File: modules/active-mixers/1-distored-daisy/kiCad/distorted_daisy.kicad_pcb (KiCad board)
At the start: 2 copper layers, 90 x 111 mm, 79 parts, among them J1 INPUT_1, J2 INPUT_2, J3 INPUT_3, J4 INPUT_4, J5 OUTPUT, J6 INV_OUT, Q1 BC547, Q2 BC547, Q3 BC547, Q4 BC547, Q5 BC547, U1 TL074

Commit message: add gerber files and ZIPs for V2
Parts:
- moved D3 9.00 mm to (101.0, 71.0)
- moved D4 9.00 mm to (101.0, 89.0)
- moved D5 9.00 mm to (101.0, 107.0)
- moved D6 9.00 mm to (101.0, 125.0)
- moved D7 9.00 mm to (111.0, 148.0)
- moved H1 9.00 mm to (111.0, 100.0)
- moved H10 9.00 mm to (127.5, 53.5)
- moved H12 9.00 mm to (127.2, 157.2)
- moved H4 9.00 mm to (103.0, 158.0)
- moved H7 9.00 mm to (94.5, 53.5)
- moved H8 9.00 mm to (94.8, 157.2)
- moved J1 9.00 mm to (101.0, 62.0)
- moved J2 9.00 mm to (101.0, 80.0)
- moved J3 9.00 mm to (101.0, 98.0)
- moved J4 9.00 mm to (101.0, 116.0)
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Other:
- board size 90 x 111 mm -> 81 x 111 mm

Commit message: cleaning up the main readme, update for 3340-vco
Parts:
- D3: value LED_IN_1 -> RED_IN_1_20mA
- D4: value LED_IN_2 -> RED_IN_2_20mA
- D5: value LED_IN_3 -> RED_IN_3_20mA
- D6: value LED_IN_4 -> RED_IN_4_20mA
- D7: value LED_OUT -> YELLOW_OUT_20mA
- J6: value INV_OUT -> DIST_OUT
- R12, R19, R3, R6, R9: value 1K -> 680R
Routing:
- added copper zone on F.Cu, net (none)
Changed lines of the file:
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@@
 			)
 		)
-		(property "Value" "LED_IN_4"
+		(property "Value" "RED_IN_4_20mA"
 			(at 0 3.96 0)
 			(layer "F.Fab")
@@
 			)
 		)
-		(property "Value" "LED_OUT"
+		(property "Value" "YELLOW_OUT_20mA"
 			(at 0 3.96 0)
 			(layer "F.Fab")
@@
 			)
 		)
-		(property "Value" "LED_IN_2"
+		(property "Value" "RED_IN_2_20mA"
 			(at 0 3.96 0)
 			(layer "F.Fab")
@@
 			)
 		)
-		(property "Value" "INV_OUT"
+		(property "Value" "DIST_OUT"
 			(at 0 9.3 -90)
 			(layer "F.Fab")
@@
 			)
 		)
-		(model "/Users/lennartquerter/Documents/KiCad/8.0/3dmodels/WQP-PJ398SM.step"
+		(model "/Users/lennart.querter/Documents/KiCad/8.0/3dmodels/WQP-PJ398SM.step"
 			(offset
 				(xyz 0 0 0)
@@
 			(pintype "passive")
 		)
-		(model "/Users/lennartquerter/Documents/KiCad/8.0/3dmodels/P0915N-EC15BR10K.stp"
+		(model "/Users/lennart.querter/Documents/KiCad/8.0/3dmodels/P0915N-EC15BR10K.stp"
 			(offset
 				(xyz 0 0 10)
@@
 			)
 		)
-		(model "/Users/lennartquerter/Documents/KiCad/8.0/3dmodels/WQP-PJ398SM.step"
+		(model "/Users/lennart.querter/Documents/KiCad/8.0/3dmodels/WQP-PJ398SM.step"
 			(offset
 				(xyz 0 0 0)
@@
 			)
 		)
-		(model "/Users/lennartquerter/Documents/KiCad/8.0/3dmodels/WQP-PJ398SM.step"
+		(model "/Users/lennart.querter/Documents/KiCad/8.0/3dmodels/WQP-PJ398SM.step"
 			(offset
 				(xyz 0 0 0)
@@
 			)
 		)
-		(model "/Users/lennartquerter/Documents/KiCad/8.0/3dmodels/WQP-PJ398SM.step"
+		(model "/Users/lennart.querter/Documents/KiCad/8.0/3dmodels/WQP-PJ398SM.step"
 			(offset
 				(xyz 0 0 0)
@@
 			)
 		)
-		(property "Value" "1K"
+		(property "Value" "680R"
 			(at 5.05 2.37 0)
 			(layer "F.Fab")
@@
 			)
 		)
-		(model "/Users/lennartquerter/Documents/KiCad/8.0/3dmodels/WQP-PJ398SM.step"
+		(model "/Users/lennart.querter/Documents/KiCad/8.0/3dmodels/WQP-PJ398SM.step"
 			(offset
 				(xyz 0 0 0)
@@
 			)
 		)
-		(property "Value" "LED_IN_1"
+		(property "Value" "RED_IN_1_20mA"
 			(at 0 3.96 0)
 			(layer "F.Fab")
@@
 			(pintype "passive")
 		)
-		(model "/Users/lennartquerter/Documents/KiCad/8.0/3dmodels/P0915N-EC15BR10K.stp"
+		(model "/Users/lennart.querter/Documents/KiCad/8.0/3dmodels/P0915N-EC15BR10K.stp"
 			(offset
 				(xyz 0 0 10)
@@
 			)
 		)
-		(property "Value" "LED_IN_3"
+		(property "Value" "RED_IN_3_20mA"
 			(at 0 3.96 0)
 			(layer "F.Fab")
@@
 			)
 		)
-		(property "Value" "1K"
+		(property "Value" "680R"
 			(at 5.05 2.37 0)
 			(layer "F.Fab")
@@
 			)
 		)
-		(property "Value" "1K"
+		(property "Value" "680R"
 			(at 5.05 2.37 0)
 			(layer "F.Fab")
@@
 			(pintype "passive")
 		)
-		(model "/Users/lennartquerter/Documents/KiCad/8.0/3dmodels/P0915N-EC15BR10K.stp"
+		(model "/Users/lennart.querter/Documents/KiCad/8.0/3dmodels/P0915N-EC15BR10K.stp"
 			(offset
 				(xyz 0 0 10)
@@
 			)
 		)
-		(property "Value" "1K"
+		(property "Value" "680R"
 			(at 5.05 2.37 0)
 			(layer "F.Fab")
@@
 			)
 		)
-		(model "/Users/lennartquerter/Documents/KiCad/8.0/3dmodels/WQP-PJ398SM.step"
+		(model "/Users/lennart.querter/Documents/KiCad/8.0/3dmodels/WQP-PJ398SM.step"
 			(offset
 				(xyz 0 0 0)
@@
 			)
 		)
-		(property "Value" "1K"
+		(property "Value" "680R"
 			(at 5.05 2.37 0)
 			(layer "F.Fab")
@@
 			(pintype "passive")
 		)
-		(model "/Users/lennartquerter/Documents/KiCad/8.0/3dmodels/P0915N-EC15BR10K.stp"
+		(model "/Users/lennart.querter/Documents/KiCad/8.0/3dmodels/P0915N-EC15BR10K.stp"
 			(offset
 				(xyz 0 0 10)
@@
 			(pintype "passive")
 		)
-		(model "/Users/lennartquerter/Documents/KiCad/8.0/3dmodels/P0915N-EC15BR10K.stp"
+		(model "/Users/lennart.querter/Documents/KiCad/8.0/3dmodels/P0915N-EC15BR10K.stp"
 			(offset
 				(xyz 0 0 10)
@@
 	)
 	(zone
+		(net 0)
+		(net_name "")
+		(layer "F.Cu")
+		(hatch edge 0.5)
+		(priority 1)
+		(connect_pads
+			(clearance 0.5)
+		)
+		(min_thickness 0.25)
+		(filled_areas_thickness no)
+		(fill yes
+			(thermal_gap 0.5)
+			(thermal_bridge_width 0.5)
+			(island_removal_mode 1)
+			(island_area_min 10)
+		)
+		(polygon
+			(pts
+				(xy 45 45) (xy 135 45) (xy 135 165) (xy 45 165)
+			)
+		)
+	)
+	(zone

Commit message: final versions of PCB for modules
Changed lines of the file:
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@@
 			(at 0 -4.2 0)
 			(layer "F.SilkS")
+			(hide yes)
 			(effects
 				(font
@@
 			(at 0 -4.2 0)
 			(layer "F.SilkS")
+			(hide yes)
 			(effects
 				(font
@@
 			(at -4 3 0)
 			(layer "F.SilkS")
+			(hide yes)
 			(effects
 				(font
@@
 			(at 0 -4.2 0)
 			(layer "F.SilkS")
+			(hide yes)
 			(effects
 				(font
@@
 			(at 0 -4.2 0)
 			(layer "F.SilkS")
+			(hide yes)
 			(effects
 				(font
@@
 			(at 0 -4.2 0)
 			(layer "F.SilkS")
+			(hide yes)
 			(effects
 				(font
@@
 			(at 0 -4.2 0)
 			(layer "F.SilkS")
+			(hide yes)
 			(effects
 				(font
@@
 			(at 3.75 3 0)
 			(layer "F.SilkS")
+			(hide yes)
 			(effects
 				(font
@@
 	)
 	(gr_text "DISTORTED_OUTPUT"
-		(at 97 154.5 0)
+		(at 97 154.3 0)
 		(layer "F.SilkS")
 		(effects
@@
 	)
 	(gr_text "OUTPUT"
-		(at 118.5 154.5 0)
+		(at 115.8 154.3 0)
 		(layer "F.SilkS")
 		(effects

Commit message: add panels, redo gerbers for distorted daisy
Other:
- board text added: "JLCJLCJLCJLC"
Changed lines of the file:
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@@
+		)
+	)
+	(gr_text "JLCJLCJLCJLC"
+		(at 77 91 90)
+		(layer "F.SilkS")
+		(effects
+			(font
+				(size 1 1)
+				(thickness 0.15)
+			)
+			(justify left bottom)
 		)
 	)

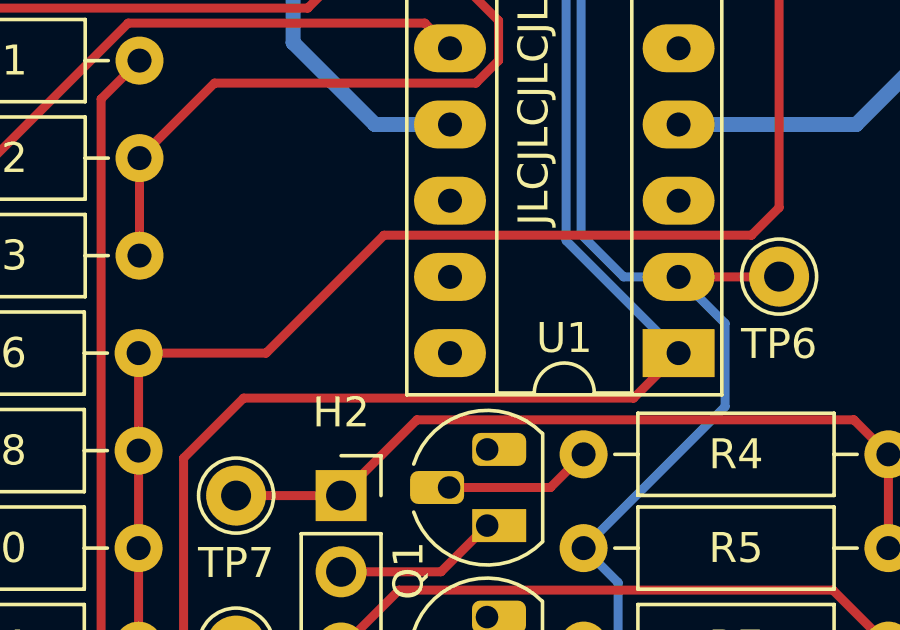
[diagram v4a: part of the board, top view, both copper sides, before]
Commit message: finish all panels, update build status, add ibom and small fixes
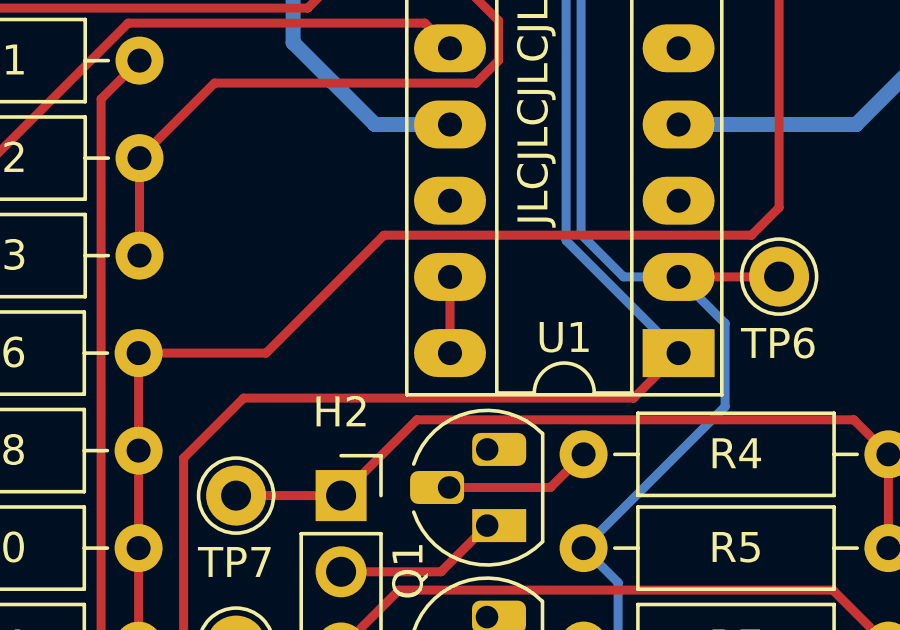
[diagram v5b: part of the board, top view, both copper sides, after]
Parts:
- R1, R2: value 10 -> 10R
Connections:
- U1 pad 12: unconnected-(U1D-+-Pad12) -> GNDREF
- U1 pad 13: unconnected-(U1D---Pad13) -> Net-(U1D--)
- U1 pad 14: unconnected-(U1-Pad14) -> Net-(U1D--)
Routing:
- net Net-(U1D--): track 0.00 -> 2.54 mm
